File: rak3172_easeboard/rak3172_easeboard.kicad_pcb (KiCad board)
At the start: 4 copper layers, 50 x 60 mm, 40 parts, among them J1 Conn_Coaxial, J2 USB_C_Receptacle, SW1 SW_Push, SW2 SW_Push, U1 RAK3172, U2 FT232RL, U3 SPX3819

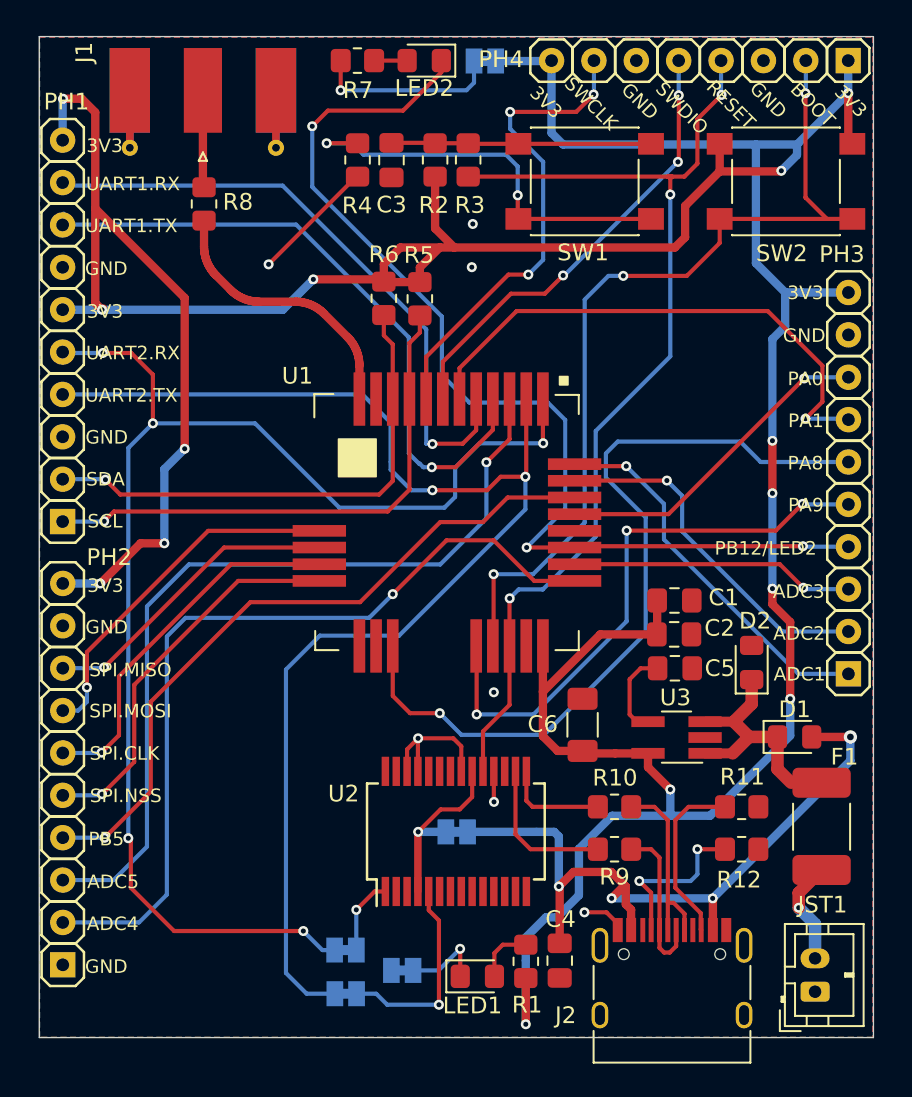
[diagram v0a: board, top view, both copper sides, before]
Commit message: Update antenna trace. Added BOM
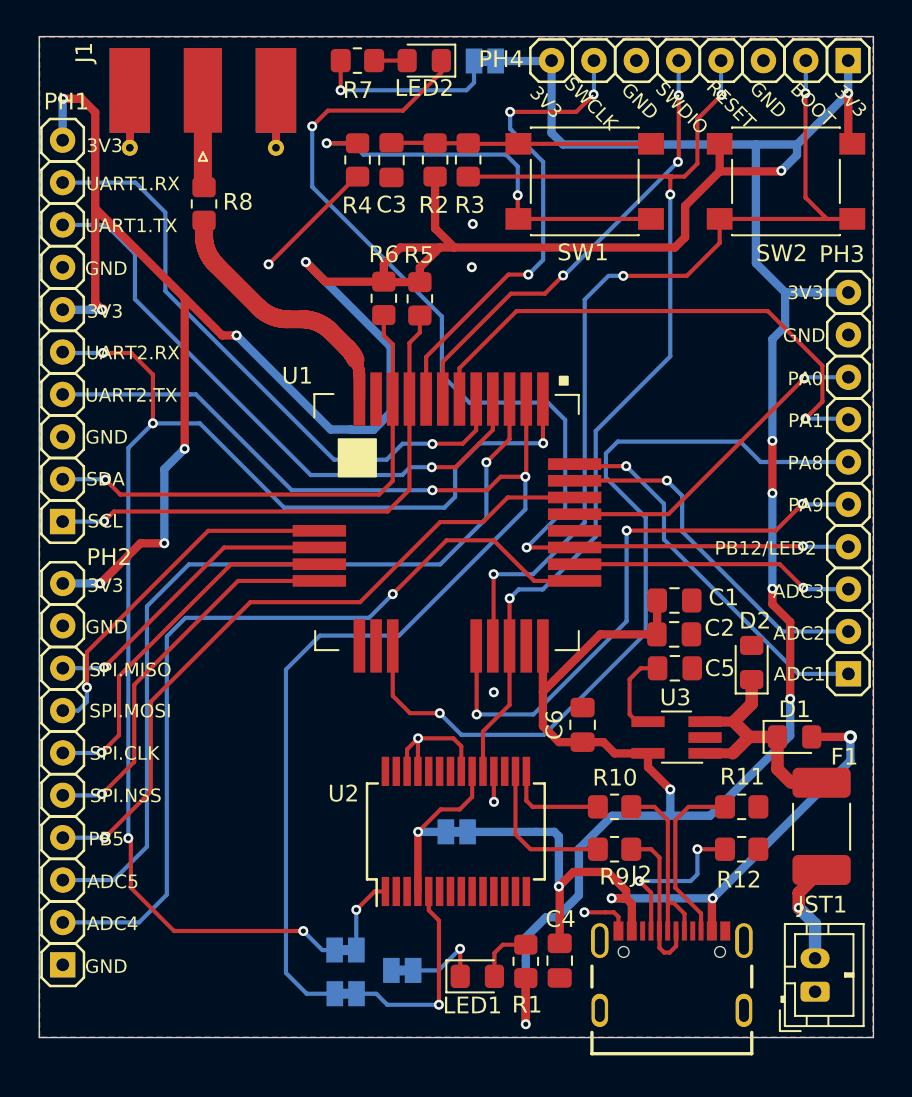
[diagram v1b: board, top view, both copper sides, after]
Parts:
- C6: footprint rak3172_easeboard:C_1206_3216Metric_Pad1.33x1.80mm_HandSolder -> rak3172_easeboard:C_0805_2012Metric_Pad1.18x1.45mm_HandSolder
- J2: value USB_C_Receptacle -> USB_C_Receptacle_Simply; footprint rak3172_easeboard:USB_C_Receptacle_HRO_TYPE-C-31-M-12 -> rak3172_easeboard:USB_C_Receptacle_12
- moved J2 0.77 mm to (154.6, 131.4)
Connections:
- J2 pad S1: Net-(J2-PadS1) -> SHIELD
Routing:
- net 3V3: track 239.1 -> 253.4 mm, vias 14 -> 15
- net UART1_TX: track 38.7 -> 36.6 mm
- net UART2_TX: track 78.7 -> 77.0 mm
- net GND: track 27.4 -> 28.5 mm
- net Net-(R8-Pad2): track 19.0 -> 18.3 mm

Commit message: UART serie protection resistors
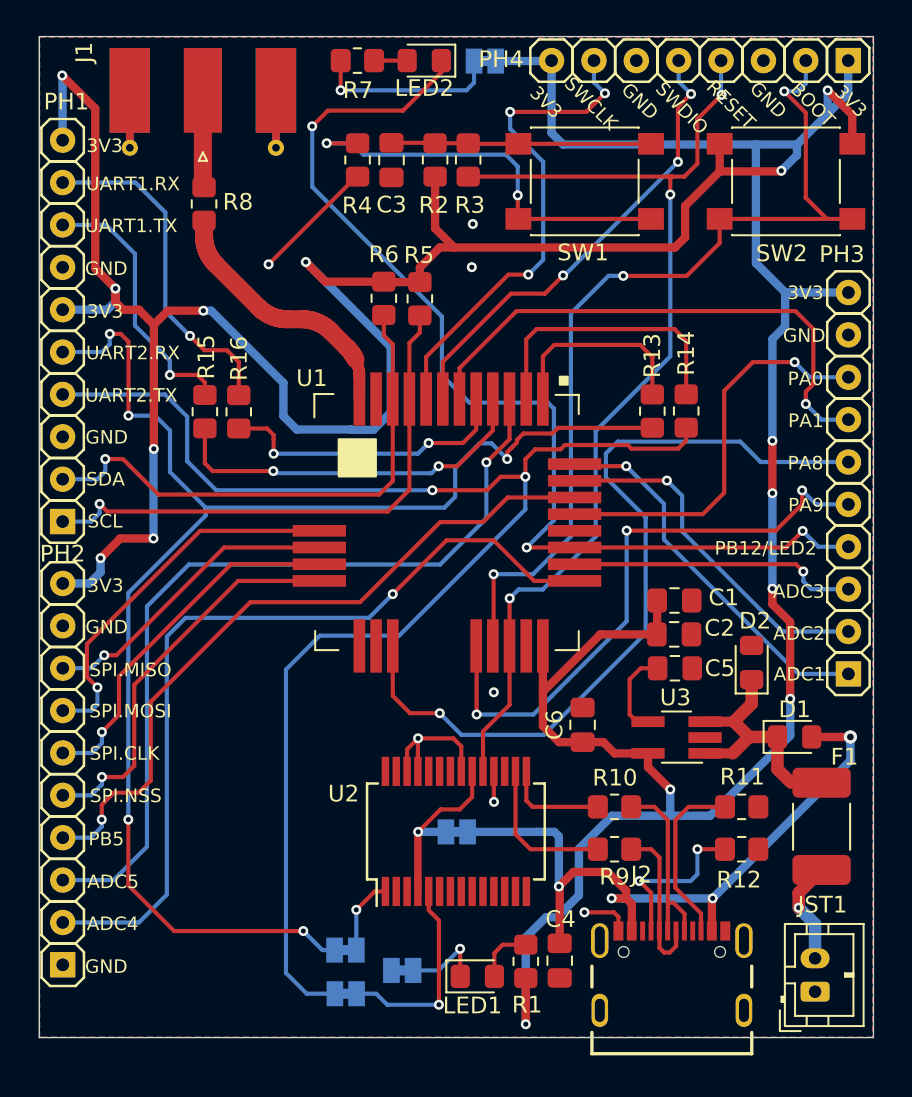
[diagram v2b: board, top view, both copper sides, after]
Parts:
- added R13: 22, rak3172_easeboard:R_0805_2012Metric_Pad1.20x1.40mm_HandSolder, F.Cu at (153.4, 95.5)
- added R14: 22, rak3172_easeboard:R_0805_2012Metric_Pad1.20x1.40mm_HandSolder, F.Cu at (155.4, 95.5)
- added R15: 22, rak3172_easeboard:R_0805_2012Metric_Pad1.20x1.40mm_HandSolder, F.Cu at (126.6, 95.5)
- added R16: 22, rak3172_easeboard:R_0805_2012Metric_Pad1.20x1.40mm_HandSolder, F.Cu at (128.6, 95.5)
- R11, R12: value 5k1 -> 5K1
- R5, R6: value 4K7 -> 5K1
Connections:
- J2 pad A8: Net-(J2-PadA8) -> (no net)
- J2 pad B8: Net-(J2-PadB8) -> (no net)
- U1 pad 1: UART2_RX -> Net-(R13-Pad2)
- U1 pad 2: UART2_TX -> Net-(R14-Pad2)
- U1 pad 4: UART1_TX -> Net-(R15-Pad2)
- U1 pad 5: UART1_RX -> Net-(R16-Pad2)
- U2 pad 10: Net-(U2-Pad10) -> (no net)
- U2 pad 11: Net-(U2-Pad11) -> (no net)
- U2 pad 12: Net-(U2-Pad12) -> (no net)
- U2 pad 13: Net-(U2-Pad13) -> (no net)
- U2 pad 14: Net-(U2-Pad14) -> (no net)
- U2 pad 17: Net-(U2-Pad17) -> (no net)
- U2 pad 2: Net-(U2-Pad2) -> (no net)
- U2 pad 22: Net-(U2-Pad22) -> (no net)
- U2 pad 23: Net-(U2-Pad23) -> (no net)
- U2 pad 27: Net-(U2-Pad27) -> (no net)
- U2 pad 28: Net-(U2-Pad28) -> (no net)
- U2 pad 3: Net-(U2-Pad3) -> (no net)
- U2 pad 6: Net-(U2-Pad6) -> (no net)
- U2 pad 9: Net-(U2-Pad9) -> (no net)
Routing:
- net Net-(R15-Pad2): track 0.00 -> 22.6 mm, vias 0 -> 2
- net UART1_TX: track 36.6 -> 16.3 mm
- net Net-(R16-Pad2): track 0.00 -> 17.9 mm, vias 0 -> 2
- net Net-(R14-Pad2): track 0.00 -> 16.9 mm
- net UART1_RX: track 37.3 -> 20.7 mm
- net Net-(R13-Pad2): track 0.00 -> 12.0 mm
- net UART2_TX: track 77.0 -> 86.1 mm
- net UART2_RX: track 81.9 -> 87.4 mm
- net PA0: track 19.8 -> 24.1 mm
- net 3V3: track 253.4 -> 250.6 mm
- net BOOT: track 53.3 -> 54.9 mm
- net I2C_SDA: track 30.7 -> 32.1 mm
- net SPI_MOSI: track 21.6 -> 22.9 mm
- net PA9: track 34.8 -> 36.0 mm
- net SWCLK: track 29.1 -> 30.0 mm
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
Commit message: Added User Button
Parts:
- added C7: 100nF, rak3172_easeboard:C_0805_2012Metric_Pad1.18x1.45mm_HandSolder, F.Cu at (126.0, 118.3)
- added R17: 100, rak3172_easeboard:R_0805_2012Metric_Pad1.20x1.40mm_HandSolder, F.Cu at (130.0, 118.3)
- added R18: 10K, rak3172_easeboard:R_0805_2012Metric_Pad1.20x1.40mm_HandSolder, F.Cu at (132.2, 118.4)
- added R19: 100, rak3172_easeboard:R_0805_2012Metric_Pad1.20x1.40mm_HandSolder, F.Cu at (128.0, 118.4)
- added SW3: SW_Push, rak3172_easeboard:SW_Push_1P1T_NO_6x6mm_H9.5mm, F.Cu at (128.9, 126.7)
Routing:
- net Net-(C7-Pad1): track 0.00 -> 24.7 mm
- net 3V3: track 250.6 -> 270.0 mm, vias 15 -> 17
- net Net-(R19-Pad1): track 0.00 -> 18.5 mm, vias 0 -> 2
- net PA9: track 36.0 -> 54.0 mm, vias 3 -> 5
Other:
- board text added: "BTN.BOOT"
- board text added: "BTN.RST"
- board text added: "PA9/BTN"
- board text added: "USR.BTN"
- board text added: "USR.LED"
- board text removed: "PA9"

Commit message: Matching Network
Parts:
- added C8_DNP1: DNP, rak3172_easeboard:C_0805_2012Metric_Pad1.18x1.45mm_HandSolder, F.Cu at (129.5, 82.4)
- moved R8 2.26 mm to (126.5, 85.3)
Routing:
- net Net-(C8_DNP1-Pad1): track 5.84 -> 10.2 mm
- net Net-(R8-Pad2): track 18.3 -> 16.4 mm

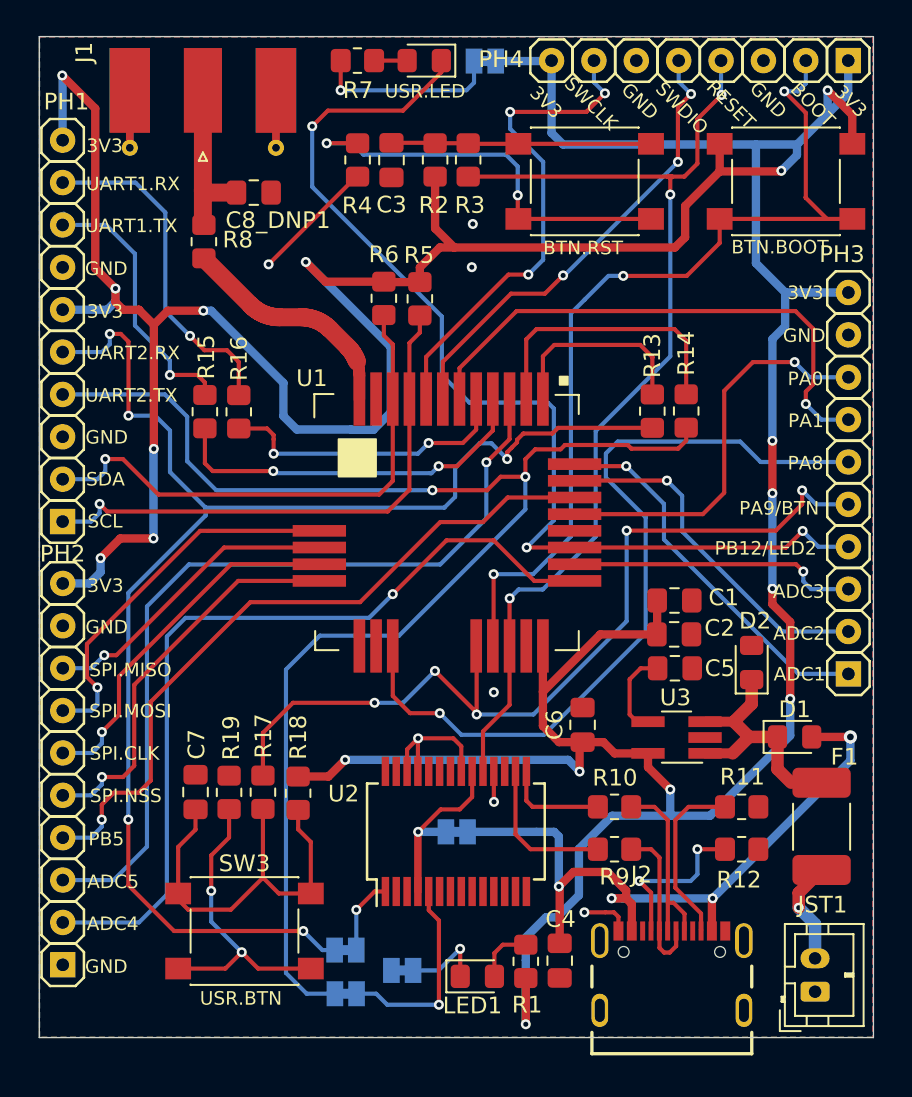
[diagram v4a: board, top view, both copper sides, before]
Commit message: Disconnect Reset from usb-serial converter
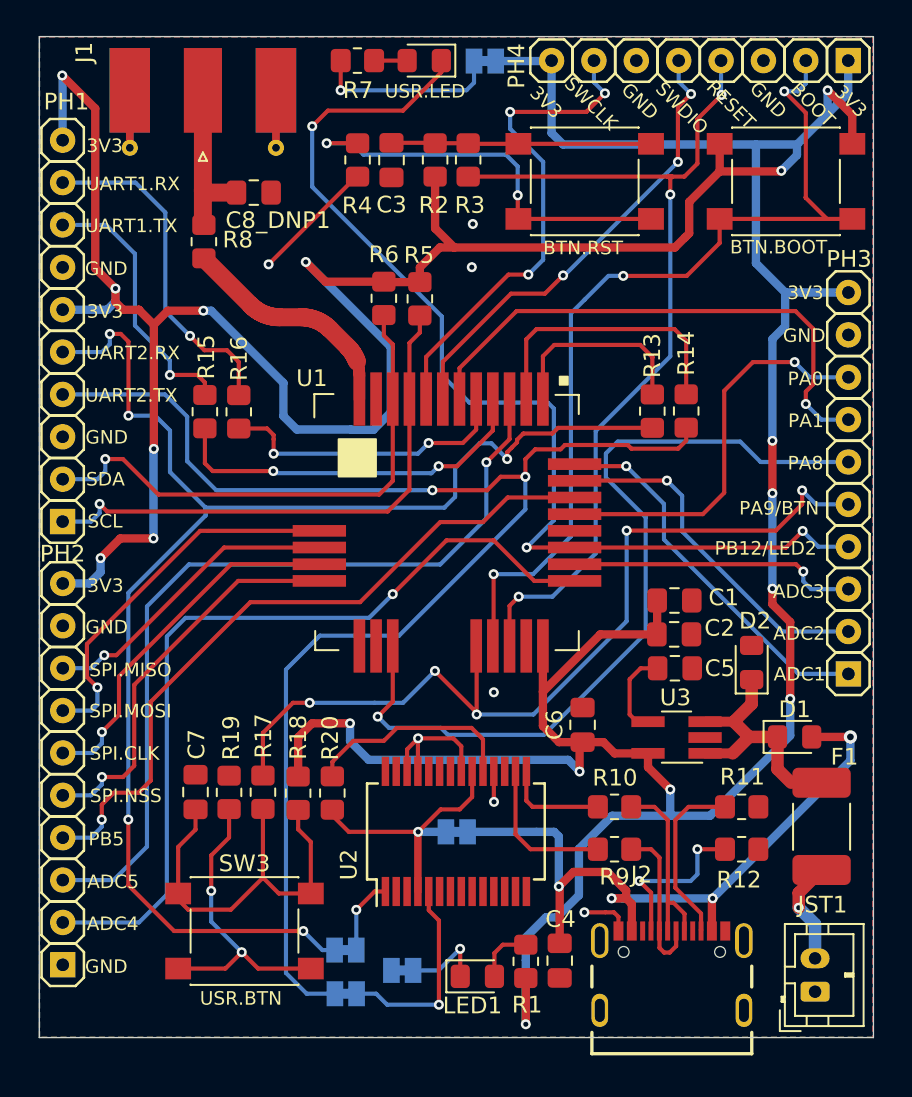
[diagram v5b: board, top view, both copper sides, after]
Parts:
- added R20: 10K, rak3172_easeboard:R_0805_2012Metric_Pad1.20x1.40mm_HandSolder, F.Cu at (134.2, 118.4)
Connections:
- U2 pad 19: RESET -> Net-(R20-Pad2)
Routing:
- net Net-(R20-Pad2): track 0.00 -> 12.9 mm
- net RESET: track 62.3 -> 54.5 mm
- net Net-(JP2-Pad1): track 10.9 -> 16.8 mm
- net 3V3: track 270.0 -> 273.8 mm
- net PA8: track 48.7 -> 50.7 mm
